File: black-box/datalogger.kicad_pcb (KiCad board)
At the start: 2 copper layers, 72.9 x 60 mm, 87 parts, among them J1 RJ12, J2 PROG, J3 PWR, J4 Micro_SD_Card_Det1, J5 USB_C_Receptacle_USB2.0_16P, J6 PWR, SW1 SW_SPST, U1 SN65HVD256D, U2 STM32F103C8Tx, U3 AP2204K-ADJ, U5 AP63200WU, Y1 8M, Y2 32.768k

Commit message: black-box: update
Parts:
- moved R15 11.5 mm to (81.0, 87.1), turned to 0 degrees
- moved R14 6.87 mm to (92.2, 87.1)
- moved R13 6.07 mm to (87.9, 87.1)
- moved C18 5.50 mm to (88.9, 91.7)
- moved C19 5.49 mm to (88.8, 94.2)
- moved R16 4.55 mm to (84.3, 87.1), turned to 180 degrees
- moved kibuzzard-6952B4C2 0.70 mm to (81.6, 69.9)
- moved kibuzzard-6952B5CA 0.70 mm to (76.9, 65.7)
- moved TP11 0.43 mm to (93.8, 73.7)
- turned J4 to 180 degrees
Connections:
- J2 pad 3: unconnected-(J2-Pin_3-Pad3) -> GND
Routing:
- net SPI1_MOSI: track 17.9 -> 30.4 mm
- net +3V3: track 166.4 -> 157.3 mm, vias 5 -> 6
- net GND: track 39.2 -> 44.3 mm
- net SD_CS: track 16.1 -> 21.2 mm
- net Net-(J4-DET): track 33.8 -> 36.8 mm
- net SPI1_MISO: track 20.6 -> 22.7 mm

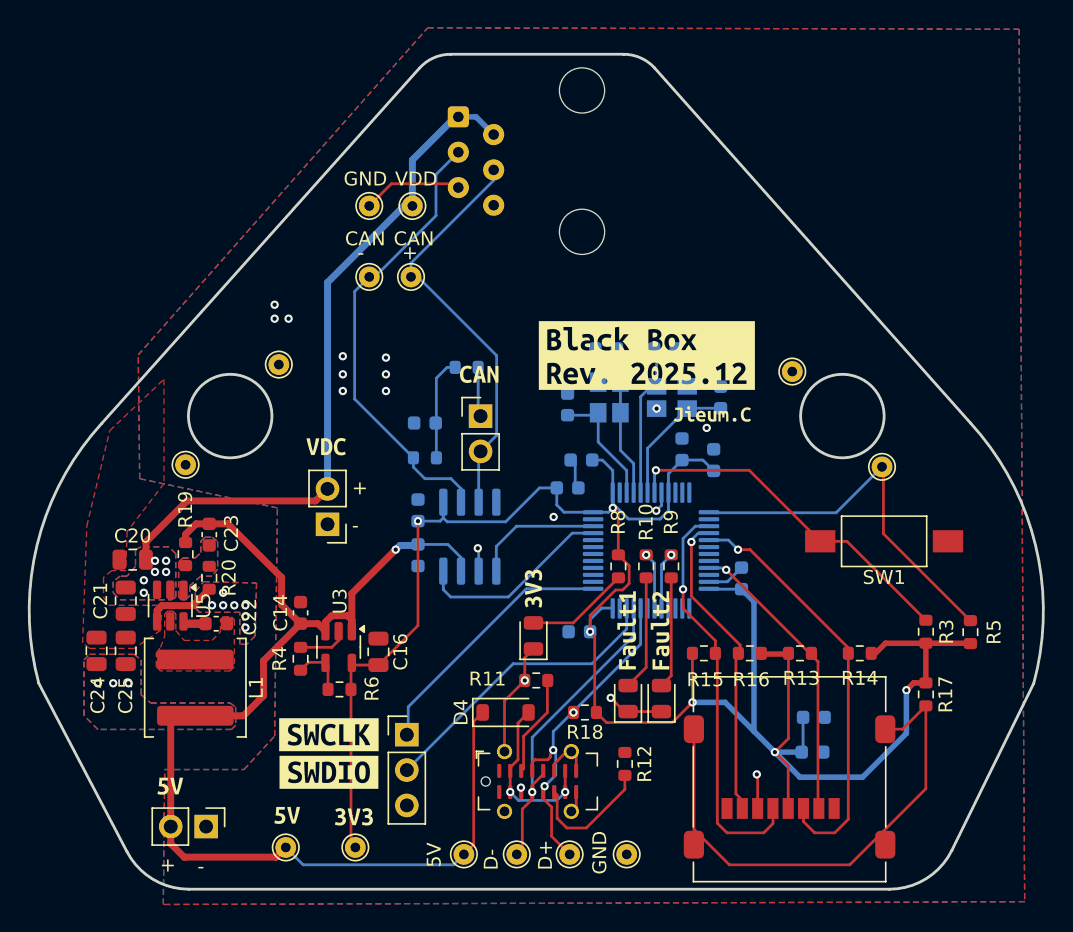
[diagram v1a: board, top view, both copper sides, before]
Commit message: black-box: add WS2812 & 3D model
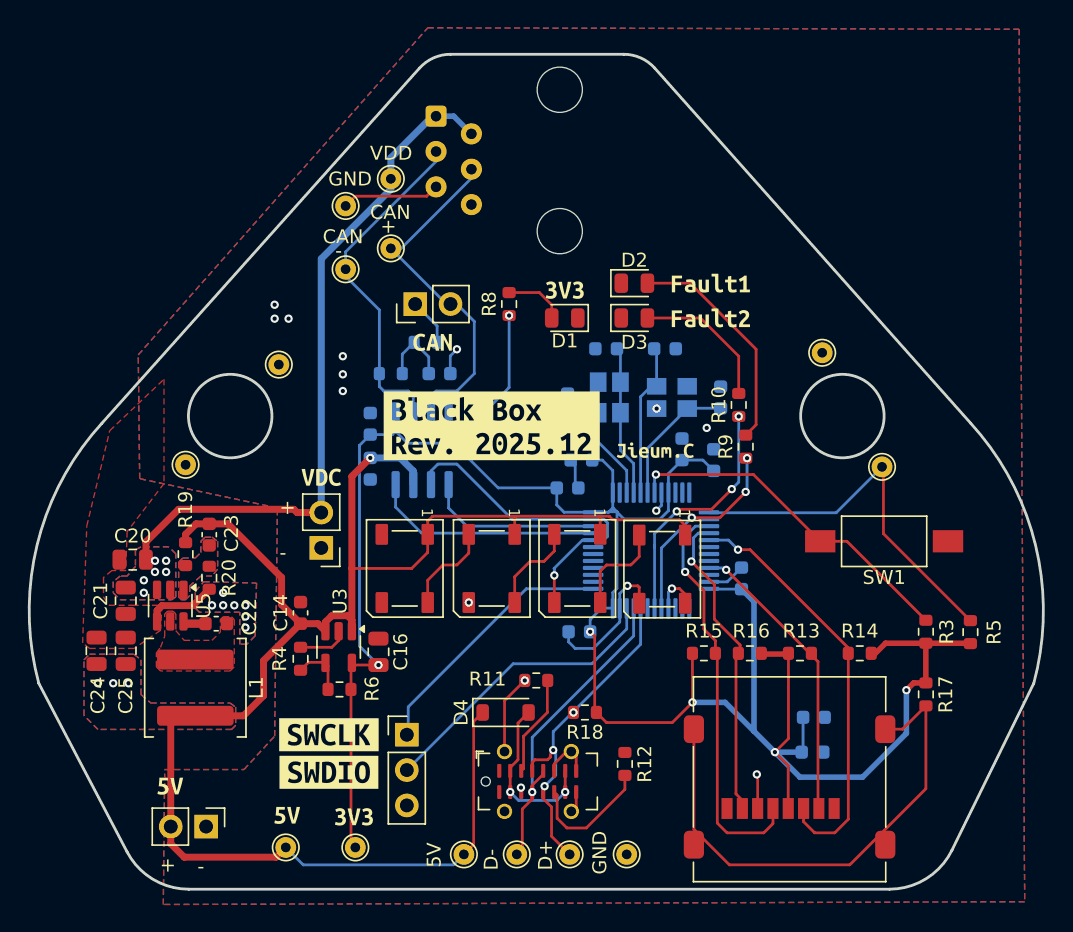
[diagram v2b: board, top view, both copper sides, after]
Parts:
- added D5: WS2812B, LED_SMD:LED_WS2812B_PLCC4_5.0x5.0mm_P3.2mm, F.Cu at (78.0, 81.0)
- added D6: WS2812B, LED_SMD:LED_WS2812B_PLCC4_5.0x5.0mm_P3.2mm, F.Cu at (71.9, 81.0)
- added D7: WS2812B, LED_SMD:LED_WS2812B_PLCC4_5.0x5.0mm_P3.2mm, F.Cu at (65.8, 81.0)
- added D8: WS2812B, LED_SMD:LED_WS2812B_PLCC4_5.0x5.0mm_P3.2mm, F.Cu at (59.5, 81.0)
- moved D2 29.9 mm to (76.0, 60.5), turned to 0 degrees
- moved D3 27.4 mm to (76.0, 63.0), turned to 0 degrees
- moved kibuzzard-6952B3A2 25.7 mm to (81.5, 60.5), turned to 0 degrees
- moved D1 23.0 mm to (71.0, 63.0), turned to 180 degrees
- moved kibuzzard-6952B3D6 22.7 mm to (81.5, 63.0), turned to 0 degrees
- moved kibuzzard-6952B17D 21.6 mm to (71.0, 61.0), turned to 0 degrees
- moved R8 20.4 mm to (67.0, 62.0), turned to 90 degrees
- moved R10 13.4 mm to (83.5, 69.2), turned to 90 degrees
- moved kibuzzard-6952B5CA 12.2 mm to (65.8, 70.8)
- moved R9 10.1 mm to (84.0, 72.2), turned to 90 degrees
- moved JP1 9.32 mm to (60.2, 62.0), turned to 90 degrees
- moved C2 7.10 mm to (57.0, 70.6)
- moved C3 7.10 mm to (57.0, 73.8)
- moved U1 7.10 mm to (60.8, 72.5)
- moved R2 6.53 mm to (58.5, 67.0)
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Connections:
- U2 pad 28: unconnected-(U2-PB15-Pad28) -> RGB
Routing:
- net +5V: track 86.0 -> 120.6 mm
- net GND: track 44.3 -> 72.1 mm, vias 25 -> 23
- net +3V3: track 157.3 -> 174.4 mm
- net LED2: track 4.10 -> 17.9 mm, vias 1 -> 3
- net LED1: track 4.14 -> 14.5 mm, vias 1 -> 3
- net Net-(D2-A): track 8.03 -> 16.3 mm
- net CAN_N: track 32.7 -> 24.7 mm
- net Net-(D5-DOUT): track 0.00 -> 7.03 mm
- net Net-(D7-DOUT): track 0.00 -> 6.71 mm
- net Net-(D6-DOUT): track 0.00 -> 6.67 mm
- net CAN_P: track 29.7 -> 25.5 mm
- net RGB: track 0.00 -> 3.30 mm, vias 0 -> 1
- net CTX: track 9.33 -> 12.6 mm
- net Net-(D1-A): track 7.44 -> 4.37 mm
- net CRX: track 14.2 -> 16.6 mm
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
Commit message: black-box: modify layout
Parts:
- moved R9 8.28 mm to (83.2, 64.0)
- moved R10 4.81 mm to (81.2, 65.0)
- moved kibuzzard-6952B17D 1.41 mm to (70.0, 60.0)
- moved kibuzzard-6952B3A2 1.35 mm to (81.0, 59.2)
- moved kibuzzard-6952B3D6 1.35 mm to (81.0, 61.8)
- moved D1 1.25 mm to (70.2, 62.0), turned to 0 degrees
- moved D2 1.25 mm to (76.0, 59.2)
- moved D3 1.00 mm to (76.0, 62.0)
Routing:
- net LED1: track 14.5 -> 23.3 mm
- net Net-(D2-A): track 16.3 -> 8.33 mm
- net LED2: track 17.9 -> 23.0 mm
- net Net-(D3-A): track 10.4 -> 5.90 mm
- net Net-(D1-A): track 4.37 -> 6.96 mm

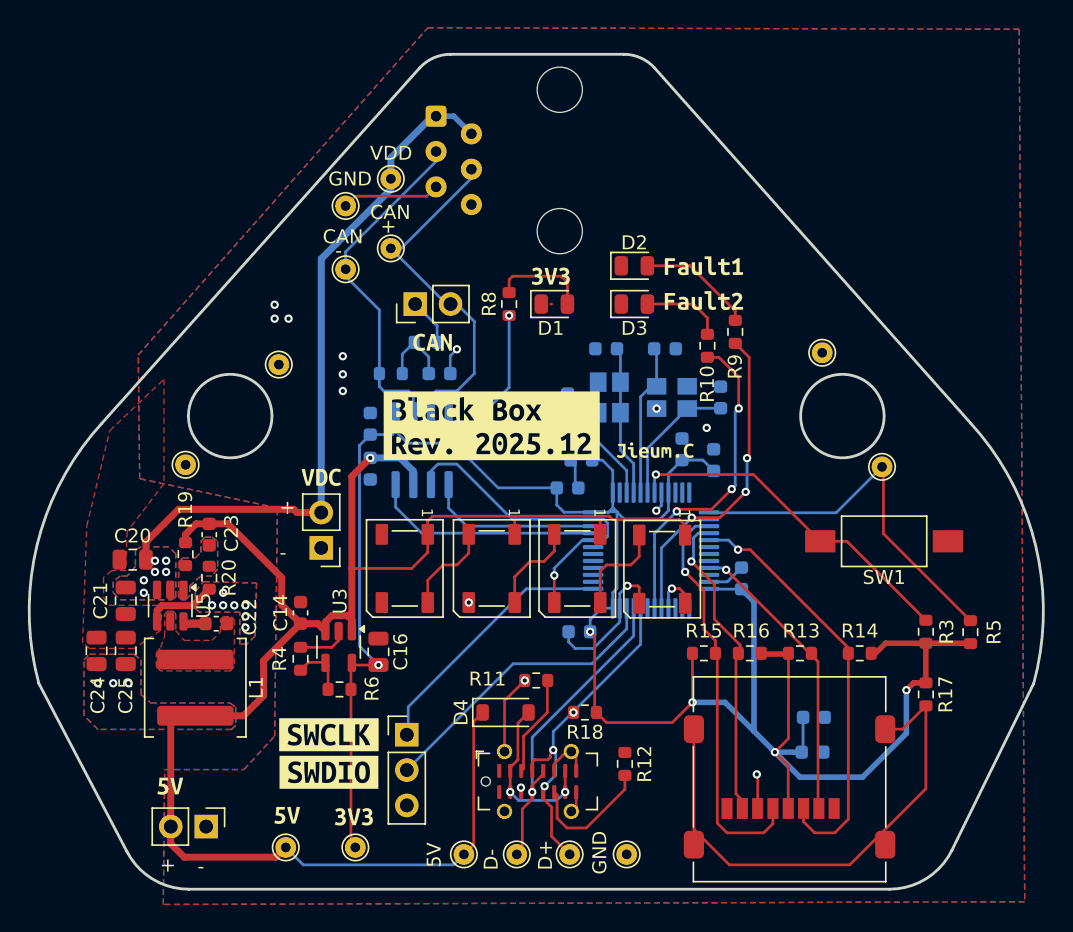
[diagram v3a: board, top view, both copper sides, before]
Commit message: V2026.01: fix: USB pin and some issues
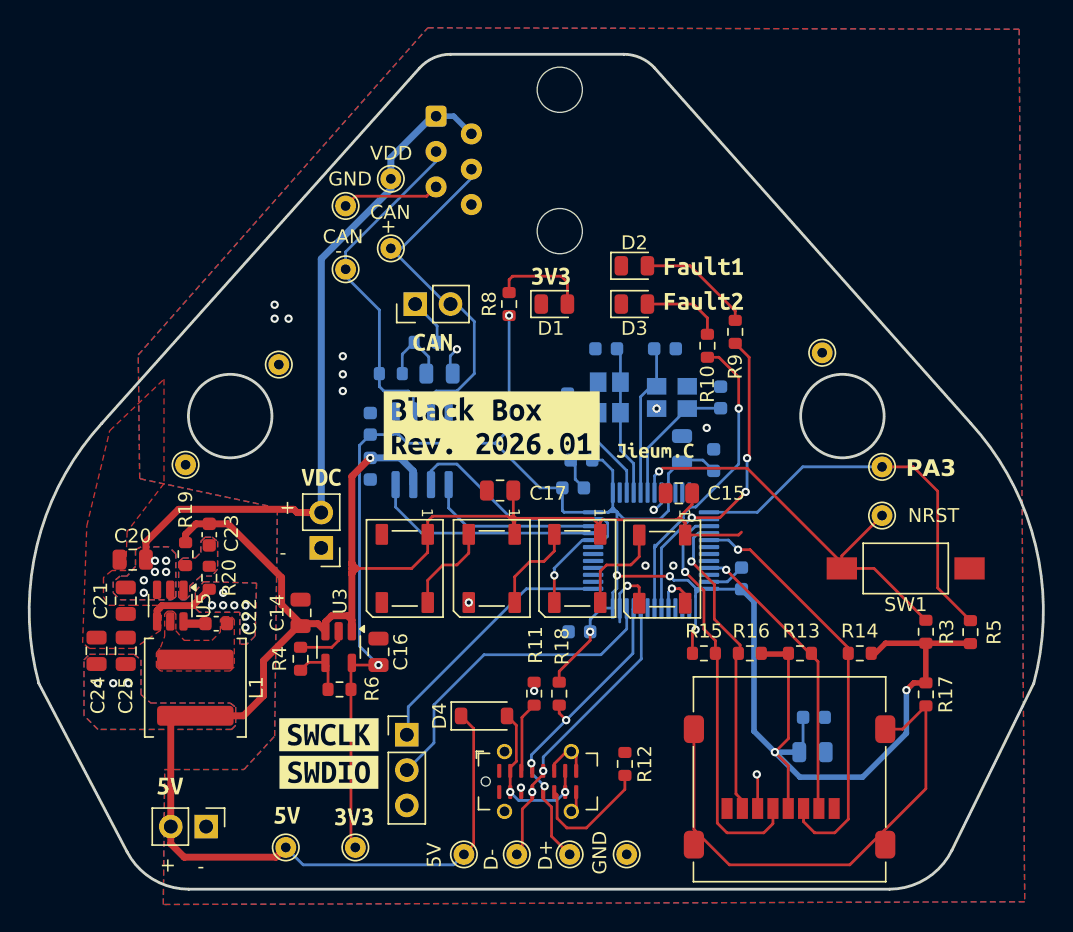
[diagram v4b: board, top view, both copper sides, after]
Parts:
- removed kibuzzard-6952B5CA: G***, kibuzzard-6952B5CA
- added C15: 1u, Capacitor_SMD:C_0805_2012Metric, F.Cu at (79.2, 75.6)
- added C17: 1u, Capacitor_SMD:C_0805_2012Metric, F.Cu at (66.3, 75.4)
- added NRST: TestPoint, TestPoint:TestPoint_THTPad_D1.5mm_Drill0.7mm, F.Cu at (93.8, 77.2)
- added kibuzzard-6977A83C: G***, kibuzzard-6977A83C, F.Cu at (65.8, 70.8)
- C1, C14, C19, C5: footprint Capacitor_SMD:C_0603_1608Metric -> Capacitor_SMD:C_0805_2012Metric
- moved SW1 2.49 mm to (95.5, 81.0)
- moved R18 2.29 mm to (70.6, 90.0), turned to -90 degrees
- moved D4 1.57 mm to (65.2, 91.6)
- moved R11 0.96 mm to (68.8, 90.0), turned to -90 degrees
- moved C12 0.40 mm to (71.6, 75.2)
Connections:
- net Net-(SW1-B) renamed NRST
- U2 pad 32: D+ -> D-
- U2 pad 33: D- -> D+
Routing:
- net +5V: track 120.6 -> 133.9 mm
- net GND: track 72.1 -> 61.2 mm, vias 23 -> 25
- net NRST: track 25.1 -> 30.7 mm
- net +3V3: track 174.4 -> 170.2 mm, vias 6 -> 8
- net Net-(J5-CC1): track 6.78 -> 5.11 mm
- net SWDIO: track 21.5 -> 23.1 mm
- net D-: track 23.0 -> 21.4 mm, vias 1 -> 2
- net Shutdown: track 27.5 -> 28.8 mm
- net LED2: track 23.0 -> 21.9 mm, vias 3 -> 1
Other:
- board text added: "PA3"

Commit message: feat: add can esd
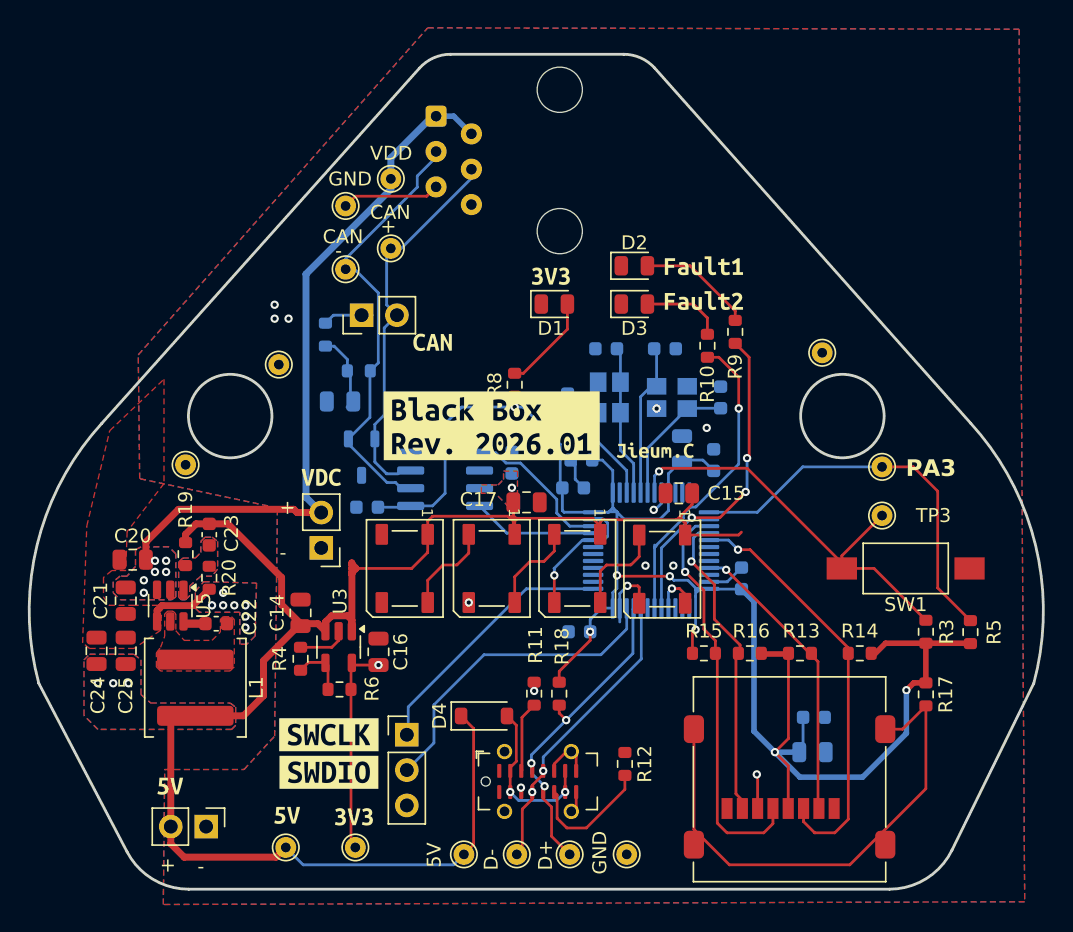
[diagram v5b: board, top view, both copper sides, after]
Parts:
- added D9: DESD2CAN2SOQ, Package_TO_SOT_SMD:TSOT-23, B.Cu at (56.4, 73.0)
- moved C3 10.2 mm to (67.2, 73.4), turned to 90 degrees
- moved C1 7.42 mm to (54.9, 69.0), turned to 180 degrees
- moved R1 7.22 mm to (53.8, 64.2), turned to -90 degrees
- moved C2 6.00 mm to (56.8, 76.6), turned to 180 degrees
- moved R8 5.81 mm to (67.4, 67.8)
- moved JP1 3.93 mm to (56.4, 62.8)
- moved U1 2.67 mm to (62.4, 74.6), turned to 180 degrees
- moved R2 2.31 mm to (56.2, 66.8), turned to 0 degrees
- moved C17 2.08 mm to (68.2, 76.2), turned to 0 degrees
- renumbered NRST to TP3
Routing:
- net +3V3: track 170.2 -> 149.7 mm
- net GND: track 61.2 -> 44.8 mm, vias 25 -> 21
- net +5V: track 133.9 -> 121.2 mm
- net CRX: track 16.6 -> 8.97 mm
- net CAN_N: track 24.7 -> 32.0 mm
- net CAN_P: track 25.5 -> 27.6 mm
- net CTX: track 12.6 -> 10.9 mm
- net VDC: track 50.1 -> 51.0 mm
